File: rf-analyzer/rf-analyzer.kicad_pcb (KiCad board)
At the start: 4 copper layers, 101.6 x 53.3 mm, 57 parts, among them J1 Conn_Coaxial, J2 RF_Shield_Two_Pieces, J3 Conn_Coaxial, U1 AD8302, U2 AD8302, U3 TLV3501_DBV, U4 HMC363S8G, U5 OPA695, U6 LTC2309_TSSOP, U7 AD8362

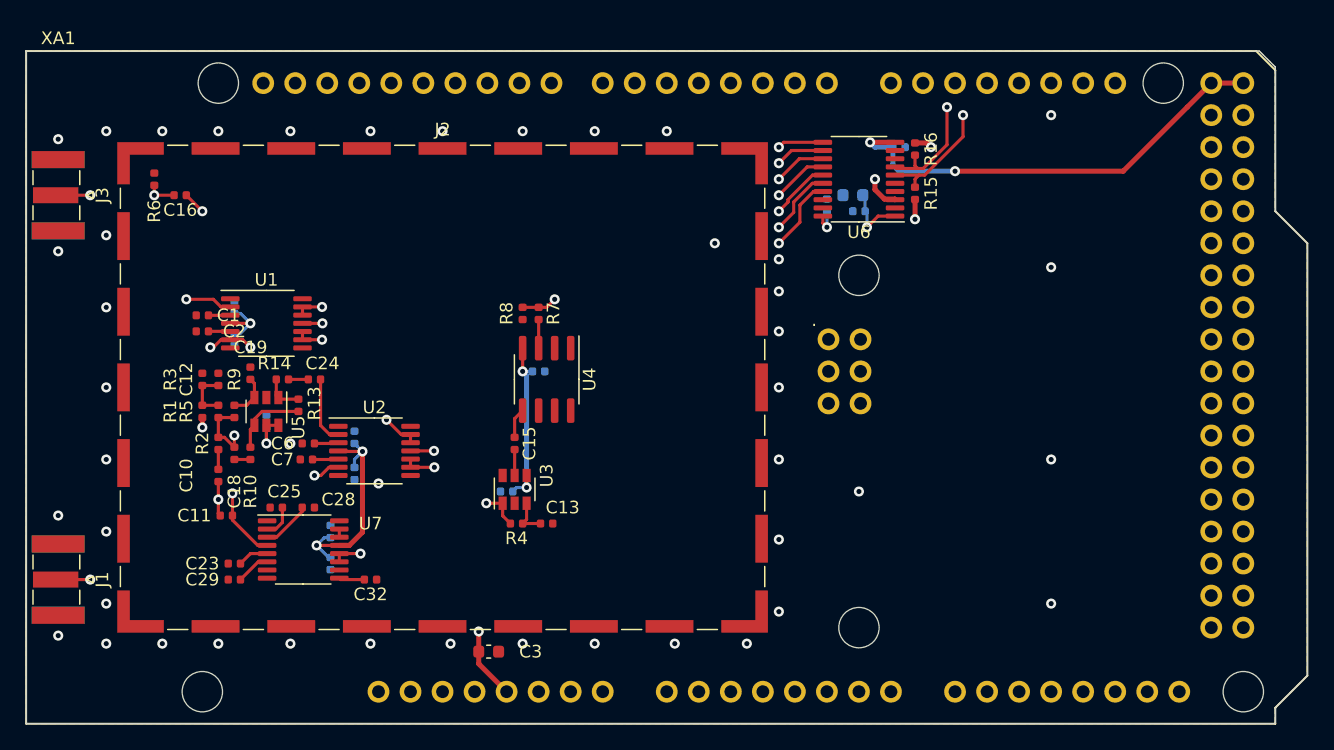
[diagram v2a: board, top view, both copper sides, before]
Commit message: Added some silkscreen info.
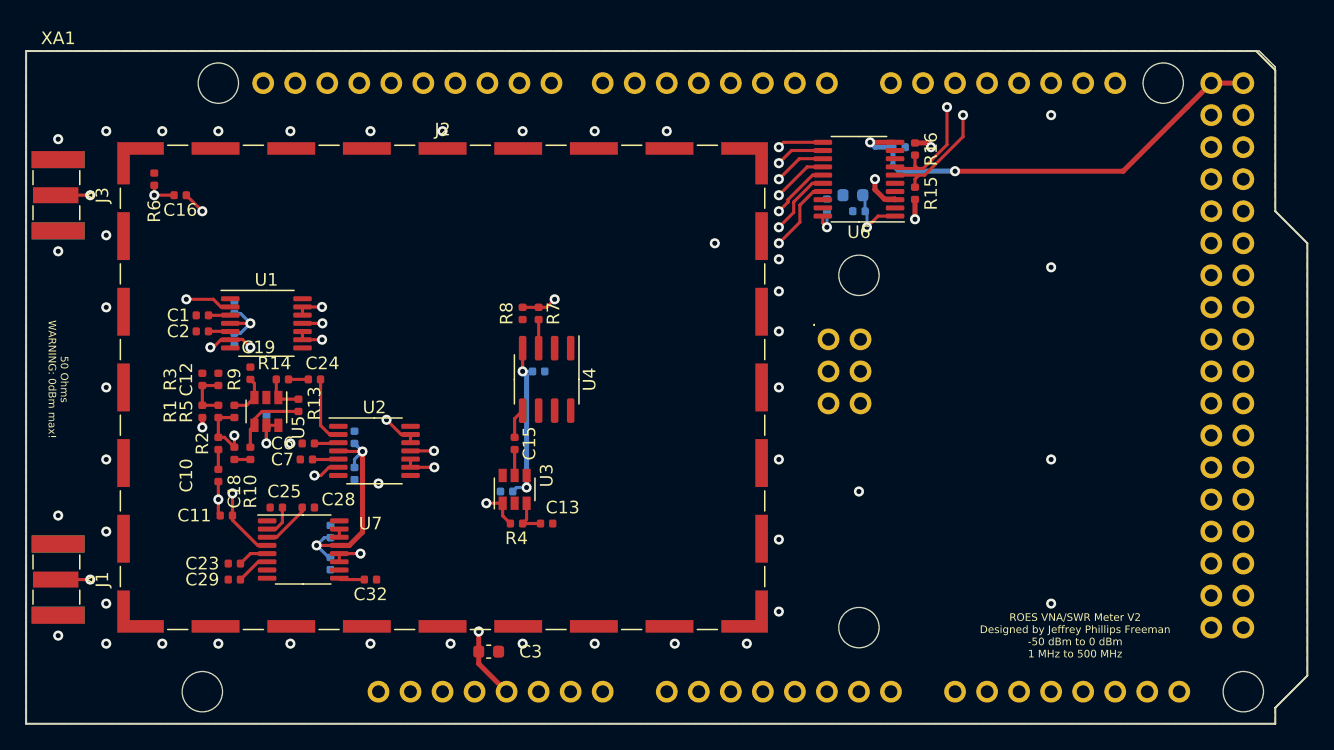
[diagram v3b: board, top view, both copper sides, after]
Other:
- board text added: "50 Ohms WARNING: 0dBm max!"
- board text added: "ROES VNA/SWR Meter V2 Designed by Jeffrey Phillips Freeman -50 dBm to 0 dBm 1 MHz to 500 MHz"
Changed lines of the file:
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@@
   (general
     (thickness 1.6)
-    (drawings 9)
+    (drawings 11)
     (tracks 416)
     (zones 0)
@@
   (page A4)
   (layers
-    (0 F.Cu signal hide)
-    (1 F2.Cu signal hide)
+    (0 F.Cu signal)
+    (1 F2.Cu signal)
     (2 B2.Cu signal)
-    (31 B.Cu signal hide)
-    (32 B.Adhes user hide)
-    (33 F.Adhes user hide)
-    (34 B.Paste user hide)
-    (35 F.Paste user hide)
-    (36 B.SilkS user hide)
-    (37 F.SilkS user hide)
-    (38 B.Mask user hide)
-    (39 F.Mask user hide)
-    (40 Dwgs.User user hide)
-    (41 Cmts.User user hide)
-    (42 Eco1.User user hide)
-    (43 Eco2.User user hide)
-    (44 Edge.Cuts user hide)
-    (45 Margin user hide)
-    (46 B.CrtYd user hide)
-    (47 F.CrtYd user hide)
-    (48 B.Fab user hide)
+    (31 B.Cu signal)
+    (32 B.Adhes user)
+    (33 F.Adhes user)
+    (34 B.Paste user)
+    (35 F.Paste user)
+    (36 B.SilkS user)
+    (37 F.SilkS user)
+    (38 B.Mask user)
+    (39 F.Mask user)
+    (40 Dwgs.User user)
+    (41 Cmts.User user)
+    (42 Eco1.User user)
+    (43 Eco2.User user)
+    (44 Edge.Cuts user)
+    (45 Margin user)
+    (46 B.CrtYd user)
+    (47 F.CrtYd user)
+    (48 B.Fab user)
     (49 F.Fab user hide)
   )
@@
     (tags capacitor)
     (attr smd)
-    (fp_text reference C19 (at -2.055 0) (layer F.SilkS)
+    (fp_text reference C19 (at -2.055 -0.635) (layer F.SilkS)
       (effects (font (size 1 1) (thickness 0.15)))
     )
@@
     (tags capacitor)
     (attr smd)
-    (fp_text reference C2 (at -2.54 0) (layer F.SilkS)
+    (fp_text reference C2 (at 1.905 0) (layer F.SilkS)
       (effects (font (size 1 1) (thickness 0.15)))
     )
@@
     (tags capacitor)
     (attr smd)
-    (fp_text reference C1 (at -2.055 0) (layer F.SilkS)
+    (fp_text reference C1 (at 1.905 0) (layer F.SilkS)
       (effects (font (size 1 1) (thickness 0.15)))
     )
@@
     )
   )
+  (gr_text "50 Ohms\nWARNING: 0dBm max!" (at 102.87 104.775 270) (layer F.SilkS)
+    (effects (font (size 0.6 0.6) (thickness 0.15)))
+  )
+  (gr_text "ROES VNA/SWR Meter V2\nDesigned by Jeffrey Phillips Freeman\n-50 dBm to 0 dBm\n1 MHz to 500 MHz" (at 183.515 125.095) (layer F.SilkS)
+    (effects (font (size 0.6 0.6) (thickness 0.15)))
+  )
   (gr_line (start 100.33 132.08) (end 100.33 78.74) (layer Edge.Cuts) (width 0.1))

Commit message: Moved around SMA connectors to pass inspection.
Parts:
- moved J1 6.07 mm to (102.9, 114.6)
- moved J3 5.36 mm to (102.9, 95.5)
- moved C16 5.08 mm to (112.5, 95.2)
- moved R6 5.08 mm to (110.5, 94.0)
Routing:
- net refl_sig: track 31.0 -> 20.8 mm
- net Net-(C10-Pad2): track 18.3 -> 15.8 mm
- net GNDA: vias 44 -> 42
